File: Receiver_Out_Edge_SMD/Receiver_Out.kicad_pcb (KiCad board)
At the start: 2 copper layers, 70 x 45 mm, 43 parts, among them J1 String1, J2 String2, J3 String3, J4 String4, J5 PGM, J6 VIN_Voltage, J7 RJ45, J8 Conn_ARM_SWD_TagConnect_TC203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, J9 XT60PW-M, SW1 Test, U2 AMS1117-5.0, U3 AM26C32IN, U4 74HCT541, U5 ATtiny1616-M

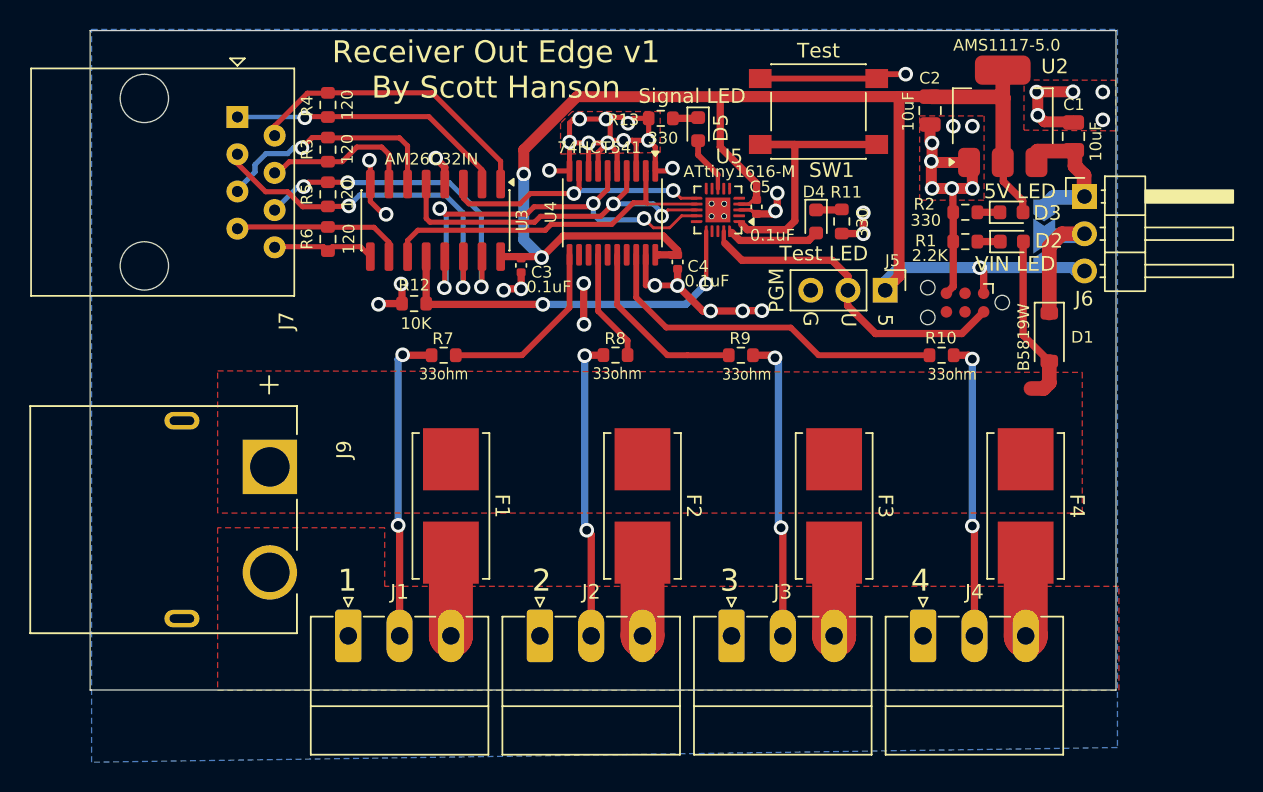
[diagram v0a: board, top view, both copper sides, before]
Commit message: update fuses on edge
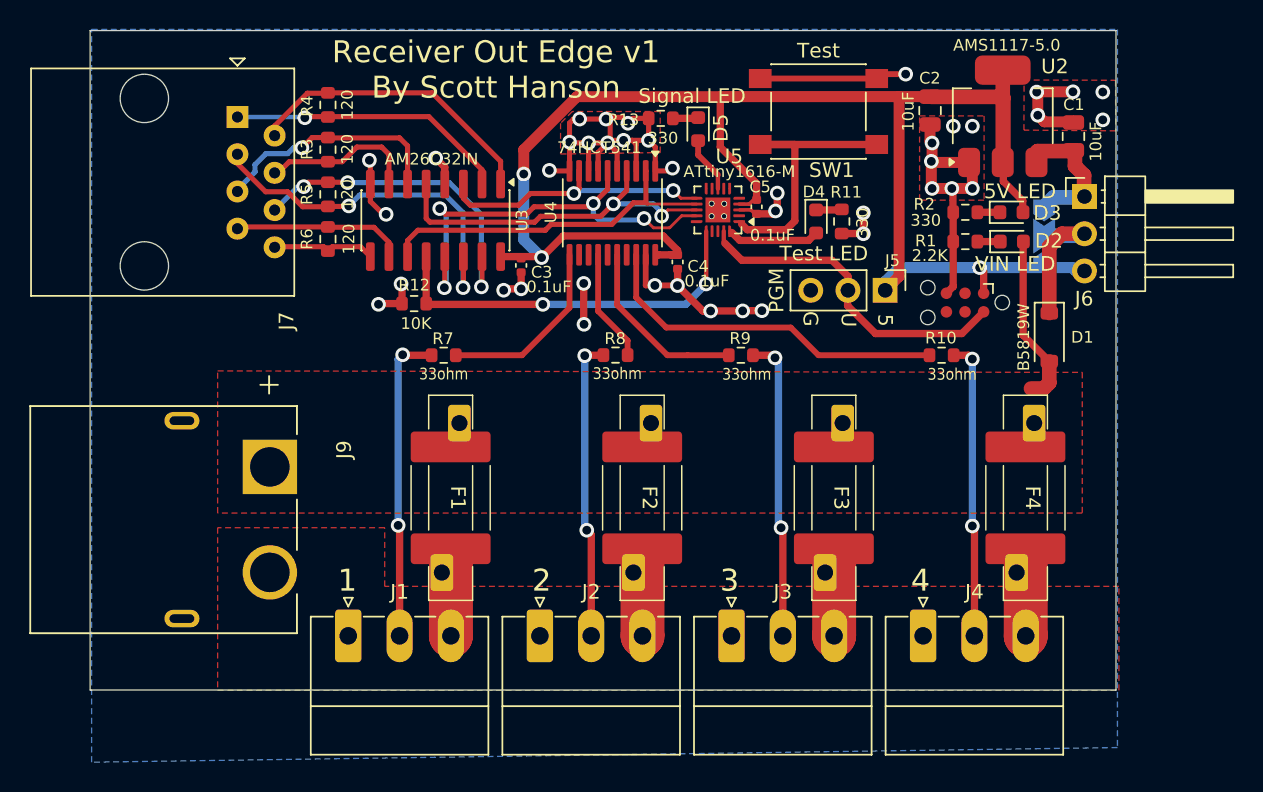
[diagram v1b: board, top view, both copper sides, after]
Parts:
- F1, F2, F3, F4: footprint Fuse:Fuseholder_Littelfuse_Nano2_154x -> Scotts:JK30-500
- moved G*** 4.74 mm to (122.8, 130.8)
- moved F1 0.56 mm to (89.2, 135.7)
- moved F2 0.56 mm to (102.3, 135.7)
- moved F3 0.56 mm to (115.4, 135.7)
- moved F4 0.56 mm to (128.4, 135.7)
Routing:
- net /Outputs/VOUT4: track 6.08 -> 5.39 mm
- net /Outputs/VOUT2: track 6.07 -> 5.39 mm

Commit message: fixes
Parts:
- F1, F2, F3, F4: footprint Scotts:JK30-500 -> Scotts:Fuse_1812_4532Metric
- moved F2 1.12 mm to (103.3, 136.1)
- moved F1 1.09 mm to (90.2, 136.1)
- moved F3 1.05 mm to (116.3, 136.1)
- moved F4 1.00 mm to (129.3, 136.1)
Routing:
- net /Outputs/VOUT2: track 5.39 -> 0.00 mm
- net /Outputs/VOUT4: track 5.39 -> 0.00 mm
- net /Outputs/VOUT3: track 5.39 -> 0.00 mm
- net /Outputs/VOUT1: track 5.39 -> 0.00 mm
- added copper zone on F.Cu, net /Outputs/VOUT1
- added copper zone on F.Cu, net /Outputs/VOUT2
- added copper zone on F.Cu, net /Outputs/VOUT3
- added copper zone on F.Cu, net /Outputs/VOUT4
